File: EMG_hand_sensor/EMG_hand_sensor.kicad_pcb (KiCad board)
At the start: 4 copper layers, 73.9 x 41.5 mm, 53 parts, among them J1 USB_C_Receptacle_USB2.0_16P, J2 Conn_01x04_Pin, J4 AudioJack3, J5 AudioJack3, J6 AudioJack3, SW1 SW_SPDT, U1 USBLC6-2SC6, U2 STM32F103C8Tx, U3 INA128, U5 INA128, U7 LT1762, U9 INA128, Y1 16MHz

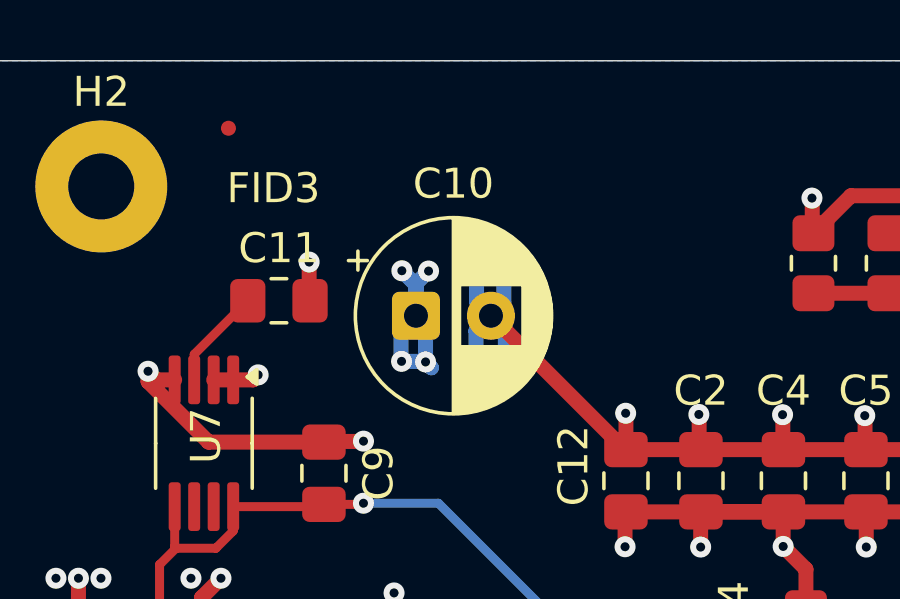
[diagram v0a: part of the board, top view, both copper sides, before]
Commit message: need to change some things because jlcpcb stock
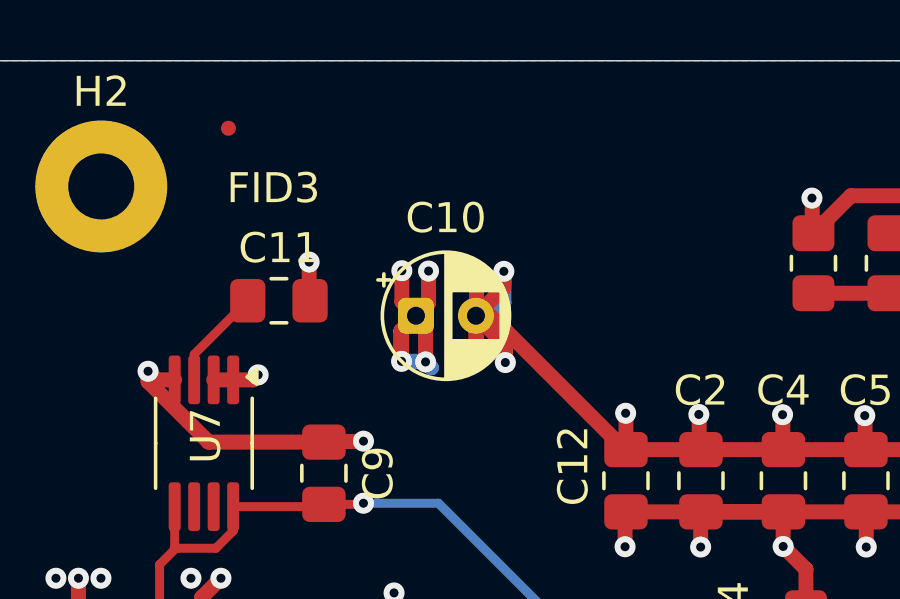
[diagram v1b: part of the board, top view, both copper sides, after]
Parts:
- C10: footprint Capacitor_THT:CP_Radial_D6.3mm_P2.50mm -> Capacitor_THT:CP_Radial_D4.0mm_P2.00mm
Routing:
- net GND: track 271.5 -> 278.3 mm
- net +3.3V: track 83.7 -> 87.1 mm

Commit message: some changes
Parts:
- FB1: footprint Resistor_SMD:R_0805_2012Metric_Pad1.20x1.40mm_HandSolder -> Ferrite_THT:LairdTech_28C0236-0JW-10
- RV1, RV2, RV3: footprint Potentiometer_SMD:Potentiometer_Bourns_3214W_Vertical -> Potentiometer_SMD:Potentiometer_Bourns_3214J_Horizontal
- moved FB1 17.4 mm to (165.2, 52.7)
- turned RV2 to 180 degrees
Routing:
- net +3.3VA: track 34.9 -> 66.1 mm, vias 4 -> 6
- net GND: track 278.3 -> 271.4 mm
- net Net-(RV2-Pad1): track 5.87 -> 11.0 mm
- net +3.3V: track 87.1 -> 88.4 mm, vias 26 -> 28

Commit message: looks good
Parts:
- FB1: footprint Ferrite_THT:LairdTech_28C0236-0JW-10 -> Ferrite_SMT:BLM21AG102BH1J
- moved FB1 2.39 mm to (165.2, 55.1)
- moved RV3 0.95 mm to (189.5, 87.5)
- moved RV1 0.45 mm to (189.5, 55.5)
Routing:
- net GND: track 271.4 -> 265.0 mm
- net /RV3_1: track 49.5 -> 54.9 mm
- net Net-(RV1-Pad3): track 10.7 -> 6.77 mm
- net +3.3V: track 88.4 -> 85.4 mm, vias 28 -> 27
- net +3.3VA: track 66.1 -> 63.7 mm, vias 6 -> 5
- net /RV3_3: track 10.9 -> 8.72 mm
- net Net-(RV1-Pad1): track 18.5 -> 19.9 mm

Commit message: done ordered
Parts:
- moved C7 14.4 mm to (169.9, 68.2), turned to 180 degrees
- moved C8 11.3 mm to (170.0, 70.5), turned to 180 degrees
- moved FB1 6.47 mm to (171.3, 57.4)
- moved R3 3.67 mm to (177.2, 56.9)
- moved R4 3.67 mm to (174.7, 56.9)
- moved FID2 1.37 mm to (199.3, 89.5)
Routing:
- net GND: track 265.0 -> 237.3 mm
- net +3.3VA: track 63.7 -> 48.2 mm
- net +1V6: track 53.0 -> 46.8 mm
- net /RV3_1: track 54.9 -> 54.1 mm
- net +3.3V: track 85.4 -> 86.1 mm
- added copper zone on F.Cu, net GND

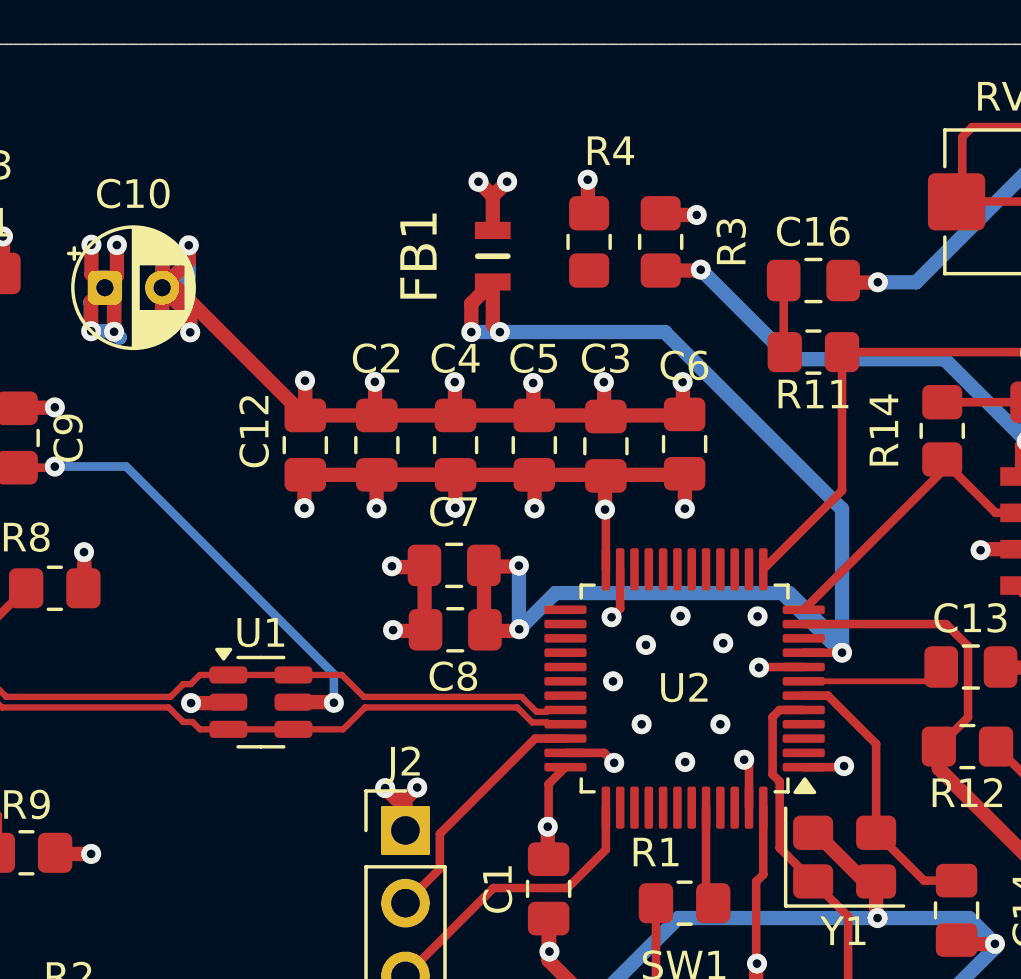
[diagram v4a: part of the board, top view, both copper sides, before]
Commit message: some changes to imporve noise
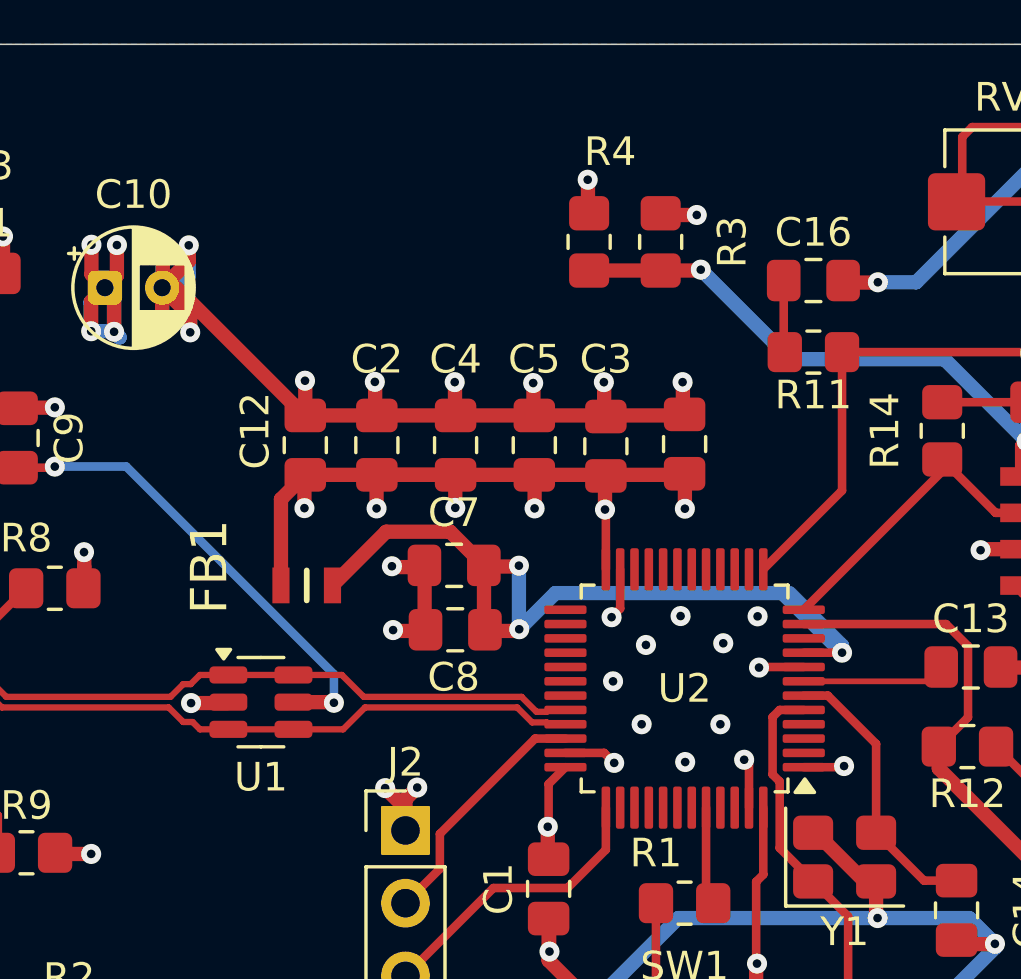
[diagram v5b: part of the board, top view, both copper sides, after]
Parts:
- moved FB1 13.2 mm to (164.8, 68.9), turned to 0 degrees
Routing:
- net +3.3VA: track 48.2 -> 30.3 mm, vias 5 -> 3
- net +1V6: track 46.8 -> 49.3 mm
- net +3.3V: track 86.1 -> 87.7 mm, vias 27 -> 25
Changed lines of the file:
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@@
 			(drillshape 0)
 			(scaleselection 1)
-			(outputdirectory "Manfacturing/")
+			(outputdirectory "Manfacturing/EMG_hand_sensor-Gerber/")
 		)
 	)
@@
 			(at 2.7125 0 180)
 			(layer "F.SilkS")
+			(hide yes)
 			(effects
 				(font
@@
 	(footprint "Ferrite_SMT:BLM21AG102BH1J"
 		(layer "F.Cu")
-		(at 171.3 57.4 -90)
+		(at 164.8 68.9)
 		(descr "BLM21_3 L=2.0 W=1.25 T=0.85")
 		(tags "Filter")
 		(property "Reference" "FB1"
-			(at 0 2.55 270)
+			(at -3.4 -0.65 90)
 			(layer "F.SilkS")
 			(effects
@@
 		)
 		(property "Value" "120R"
-			(at 0 0 270)
+			(at 0 0 0)
 			(layer "F.SilkS")
 			(hide yes)
@@
 		)
 		(property "Datasheet" ""
-			(at 0 0 270)
+			(at 0 0 0)
 			(layer "F.Fab")
 			(hide yes)
@@
 		)
 		(property "Description" "Ferrite bead"
-			(at 0 0 270)
+			(at 0 0 0)
 			(layer "F.Fab")
 			(hide yes)
@@
 		)
 		(property "MANUFACTURER" ""
-			(at 0 0 270)
+			(at 0 0 0)
 			(unlocked yes)
 			(layer "F.Fab")
@@
 		)
 		(property "MAXIMUM_PACKAGE_HEIGHT" ""
-			(at 0 0 270)
+			(at 0 0 0)
 			(unlocked yes)
 			(layer "F.Fab")
@@
 		)
 		(property "PARTREV" ""
-			(at 0 0 270)
+			(at 0 0 0)
 			(unlocked yes)
 			(layer "F.Fab")
@@
 		)
 		(property "STANDARD" ""
-			(at 0 0 270)
+			(at 0 0 0)
 			(unlocked yes)
 			(layer "F.Fab")
@@
 		)
 		(fp_line
-			(start -2.2 1.625)
-			(end -2.2 -1.625)
+			(start -2.2 -1.625)
+			(end 2.2 -1.625)
 			(stroke
 				(width 0.1)
@@
 		)
 		(fp_line
-			(start 2.2 1.625)
-			(end -2.2 1.625)
+			(start -2.2 1.625)
+			(end -2.2 -1.625)
 			(stroke
 				(width 0.1)
@@
 		)
 		(fp_line
-			(start -2.2 -1.625)
-			(end 2.2 -1.625)
+			(start 2.2 -1.625)
+			(end 2.2 1.625)
 			(stroke
 				(width 0.1)
@@
 		)
 		(fp_line
-			(start 2.2 -1.625)
-			(end 2.2 1.625)
+			(start 2.2 1.625)
+			(end -2.2 1.625)
 			(stroke
 				(width 0.1)
@@
 		)
 		(fp_line
-			(start -1 0.625)
-			(end -1 -0.625)
+			(start -1 -0.625)
+			(end 1 -0.625)
 			(stroke
 				(width 0.1)
@@
 		)
 		(fp_line
-			(start 1 0.625)
-			(end -1 0.625)
+			(start -1 0.625)
+			(end -1 -0.625)
 			(stroke
 				(width 0.1)
@@
 		)
 		(fp_line
-			(start -1 -0.625)
-			(end 1 -0.625)
+			(start 1 -0.625)
+			(end 1 0.625)
 			(stroke
 				(width 0.1)
@@
 		)
 		(fp_line
-			(start 1 -0.625)
-			(end 1 0.625)
+			(start 1 0.625)
+			(end -1 0.625)
 			(stroke
 				(width 0.1)
@@
 		)
 		(fp_text user "${REFERENCE}"
-			(at 0 0 270)
+			(at 0 0 0)
 			(layer "F.Fab")
 			(effects
@@
 		)
 		(pad "1" smd rect
-			(at -0.9 0 270)
+			(at -0.9 0)
 			(size 0.6 1.25)
 			(layers "F.Cu" "F.Mask" "F.Paste")
@@
 		)
 		(pad "2" smd rect
-			(at 0.9 0 270)
+			(at 0.9 0)
 			(size 0.6 1.25)
 			(layers "F.Cu" "F.Mask" "F.Paste")
@@
 		(tags "SOT TO_SOT_SMD")
 		(property "Reference" "U1"
-			(at 0 -2.4 0)
+			(at 0 2.6225 0)
 			(layer "F.SilkS")
 			(effects
@@
 	)
 	(segment
-		(start 171.3 59.8)
-		(end 171.55 60.05)
-		(width 0.5)
-		(layer "F.Cu")
-		(net 1)
-	)
-	(segment
-		(start 171.3 58.3)
-		(end 170.55 59.05)
+		(start 169.8115 67.024)
+		(end 170.9875 68.2)
 		(width 0.5)
 		(layer "F.Cu")
@@
 	)
 	(segment
-		(start 171.3 58.3)
-		(end 171.3 59.8)
+		(start 165.7 68.9)
+		(end 167.576 67.024)
 		(width 0.5)
 		(layer "F.Cu")
@@
 	)
 	(segment
-		(start 170.55 59.05)
-		(end 170.55 60.05)
+		(start 167.576 67.024)
+		(end 169.8115 67.024)
 		(width 0.5)
 		(layer "F.Cu")
@@
 	)
 	(via
-		(at 170.55 60.05)
-		(size 0.7)
-		(drill 0.3)
-		(layers "F.Cu" "B.Cu")
-		(free yes)
-		(net 1)
-	)
-	(via
-		(at 171.55 60.05)
-		(size 0.7)
-		(drill 0.3)
-		(layers "F.Cu" "B.Cu")
-		(free yes)
-		(net 1)
-	)
-	(via
 		(at 183.5 71.25)
 		(size 0.7)
@@
 	)
 	(segment
-		(start 177.314036 60.05)
-		(end 183.5 66.235964)
-		(width 0.5)
-		(layer "B.Cu")
-		(net 1)
-	)
-	(segment
-		(start 171.55 60.05)
-		(end 177.314036 60.05)
-		(width 0.5)
-		(layer "B.Cu")
-		(net 1)
-	)
-	(segment
-		(start 170.55 60.05)
-		(end 171.55 60.05)
-		(width 0.5)
-		(layer "B.Cu")
-		(net 1)
-	)
-	(segment
 		(start 183.5 71)
 		(end 183.5 71.25)
@@
 	)
 	(segment
-		(start 183.5 66.235964)
-		(end 183.5 71.25)
-		(width 0.5)
-		(layer "B.Cu")
-		(net 1)
-	)
-	(segment
 		(start 172.2225 70.43)
 		(end 173.4835 69.169)
@@
 	)
 	(segment
+		(start 174.665 57.9)
+		(end 177.165 57.9)
+		(width 0.5)
+		(layer "F.Cu")
+		(net 13)
+	)
+	(segment
 		(start 193.845 57.461)
 		(end 193.845 58.845)
@@
 	)
 	(segment
-		(start 171.3 56.5)
-		(end 171.3 55.3)
-		(width 0.5)
-		(layer "F.Cu")
-		(net 14)
-	)
-	(segment
 		(start 194.75 88)
 		(end 194.75 86.79)
@@
 	)
 	(segment
-		(start 189.789 67.635)
-		(end 188.375 67.635)
+		(start 163.9 68.9)
+		(end 163.9 65.8875)
 		(width 0.5)
 		(layer "F.Cu")
@@
 	)
 	(segment
-		(start 188.375 67.635)
-		(end 188.34 67.67)
+		(start 189.789 67.635)
+		(end 188.375 67.635)
 		(width 0.5)
 		(layer "F.Cu")
@@
 	)
 	(segment
-		(start 171.3 55.3)
-		(end 170.8 54.8)
+		(start 188.375 67.635)
+		(end 188.34 67.67)
 		(width 0.5)
 		(layer "F.Cu")
@@
 	)
 	(segment
-		(start 171.3 55.3)
-		(end 171.8 54.8)
-		(width 0.5)
-		(layer "F.Cu")
-		(net 14)
-	)
-	(segment
 		(start 173.22 77.33)
 		(end 173.22 78.54)
@@
 		(net 14)
 	)
+	(segment
+		(start 163.9 65.8875)
+		(end 164.75 65.0375)
+		(width 0.5)
+		(layer "F.Cu")
+		(net 14)
+	)
 	(via
 		(at 154.19 56.71)
@@
 	)
 	(via
-		(at 170.8 54.8)
-		(size 0.7)
-		(drill 0.3)
-		(layers "F.Cu" "B.Cu")
-		(free yes)
-		(net 14)
-	)
-	(via
 		(at 167.54 75.98)
 		(size 0.7)
@@
 		(size 0.7)
 		(drill 0.3)
-		(layers "F.Cu" "B.Cu")
-		(free yes)
-		(net 14)
-	)
-	(via
-		(at 171.8 54.8)
-		(size 0.7)
-		(drill 0.3)

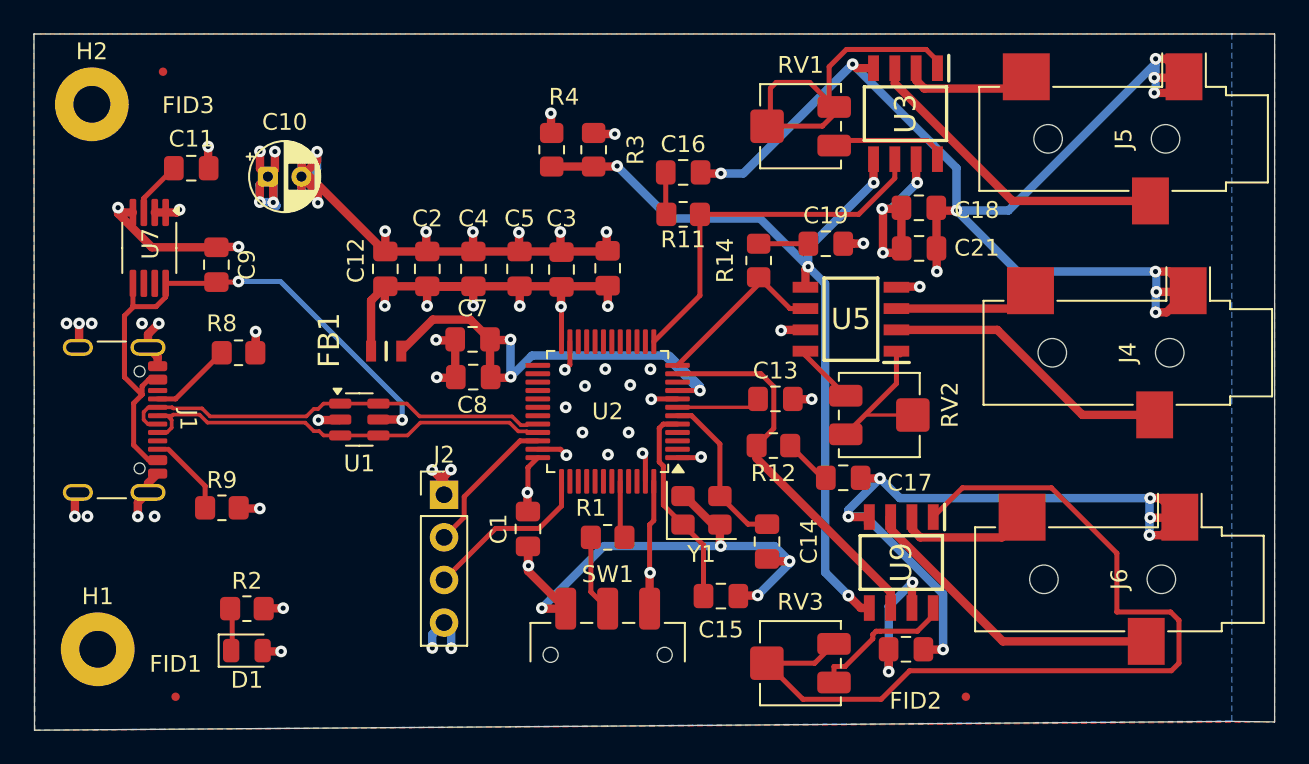
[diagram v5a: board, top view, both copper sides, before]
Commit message: updated for cheaper parts
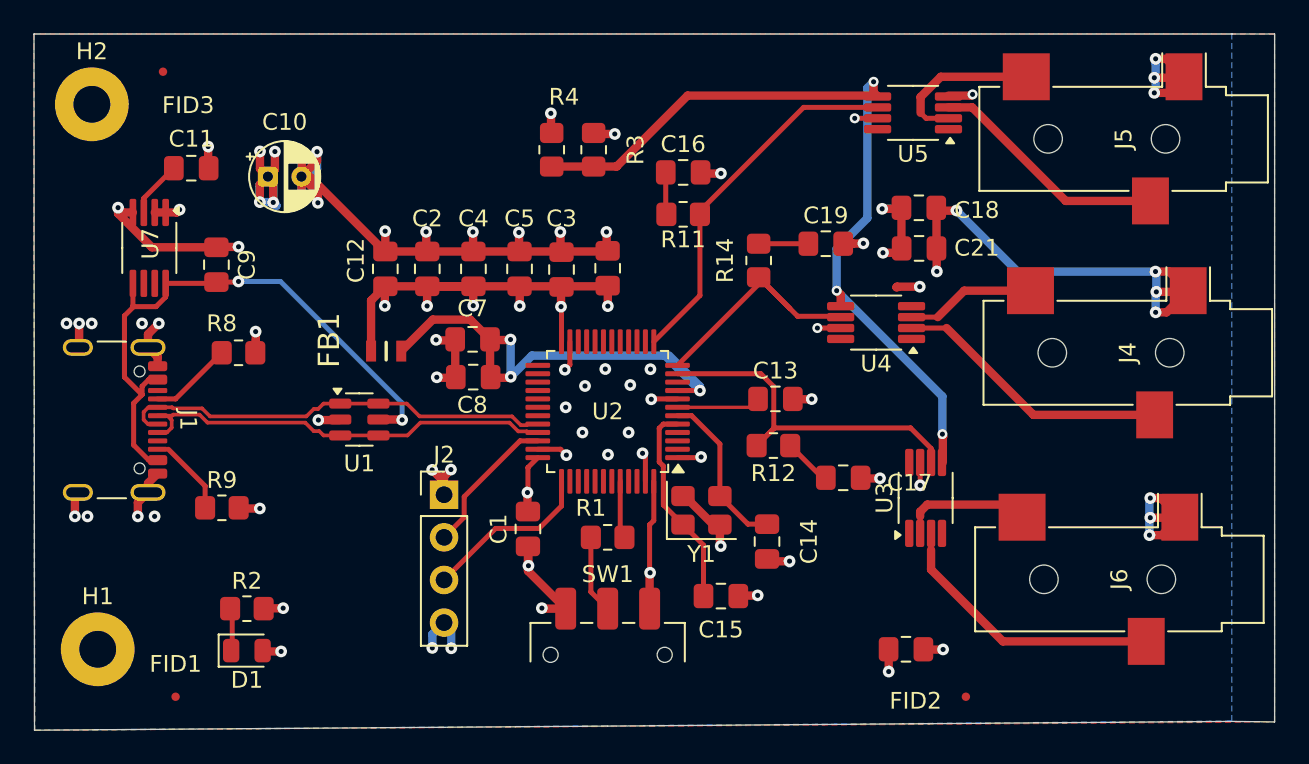
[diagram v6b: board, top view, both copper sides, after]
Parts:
- removed RV1, RV2, RV3: 500R, Potentiometer_SMD:Potentiometer_Bourns_3214J_Horizontal
- removed U9: INA128, INA:SOIC127P600X175-8N
- added U4: INA333xxDGK, Package_SO:VSSOP-8_3x3mm_P0.65mm, F.Cu at (194.0, 67.2)
- U2: value STM32F103C8Tx -> STM32F103C8T6
- U3, U5: value INA128 -> INA333xxDGK; footprint INA:SOIC127P600X175-8N -> Package_SO:VSSOP-8_3x3mm_P0.65mm
- moved U3 22.9 mm to (196.9, 77.7), turned to 90 degrees
- moved U5 12.8 mm to (196.2, 54.7)
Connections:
- U3 pad 2: /E2 -> /E6
- U3 pad 3: /E1 -> /E5
- U3 pad 6: /O4 -> /O2
- U5 pad 2: /E8 -> /E2
- U5 pad 3: /E7 -> /E1
- U5 pad 6: /O3 -> /O4
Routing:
- net GND: track 237.3 -> 149.3 mm, vias 66 -> 65
- net /RV3_1: track 54.1 -> 0.00 mm
- net Net-(U3-Rg-Pad1): track 19.9 -> 0.00 mm
- net Net-(U5-Rg-Pad1): track 11.0 -> 0.00 mm
- net +3.3V: track 87.7 -> 76.7 mm
- net /RV3_3: track 8.72 -> 0.00 mm
- net Net-(U3-Rg-Pad8): track 6.77 -> 0.00 mm
- net /O3: track 10.8 -> 15.8 mm
- net /E1: track 19.0 -> 14.3 mm
- net Net-(U5-Rg-Pad8): track 3.65 -> 0.00 mm
- net /E2: track 7.78 -> 10.5 mm
- net /E5: track 19.1 -> 17.4 mm
- net /E6: track 9.48 -> 11.0 mm
- net /E8: track 17.5 -> 16.6 mm
- net /E7: track 8.43 -> 9.25 mm
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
